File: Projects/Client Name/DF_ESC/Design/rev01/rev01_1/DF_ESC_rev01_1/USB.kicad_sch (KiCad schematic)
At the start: 9 parts, among them J8 USB_C_Receptacle_USB2.0, U10 PUSB3AB6Z

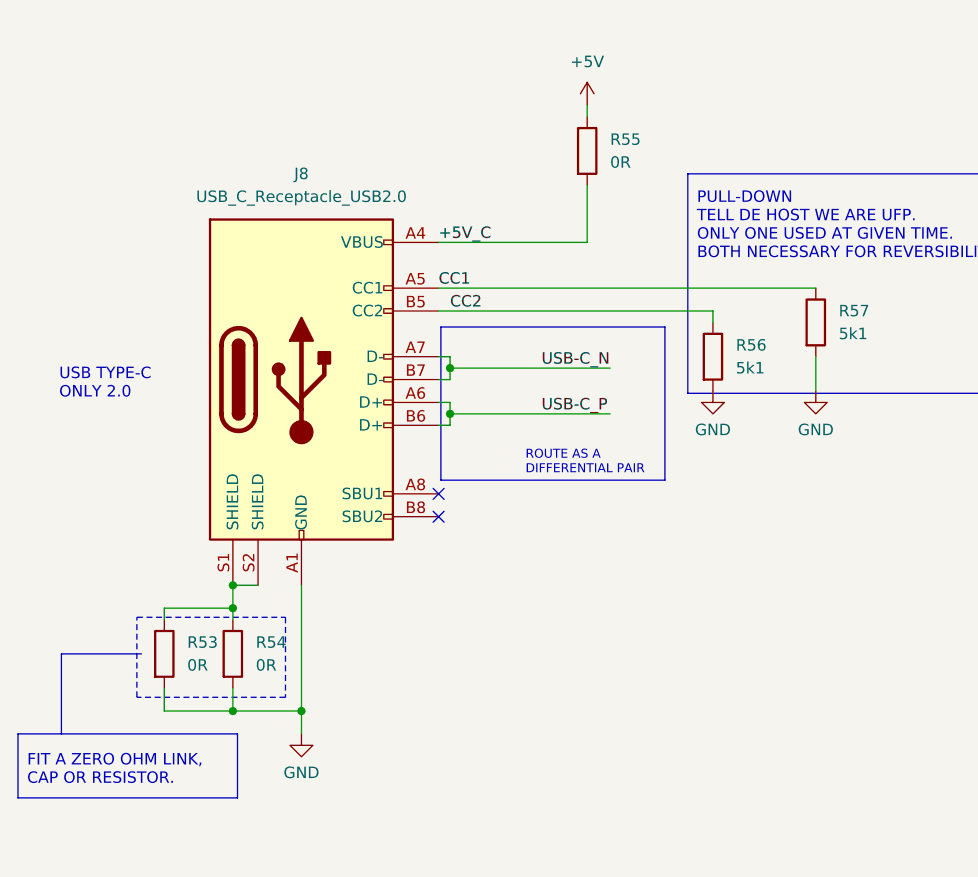
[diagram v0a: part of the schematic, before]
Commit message: update 20240427
Mejora de layout cero errores, solo falta añadir algunas reseñas en el silkscreen
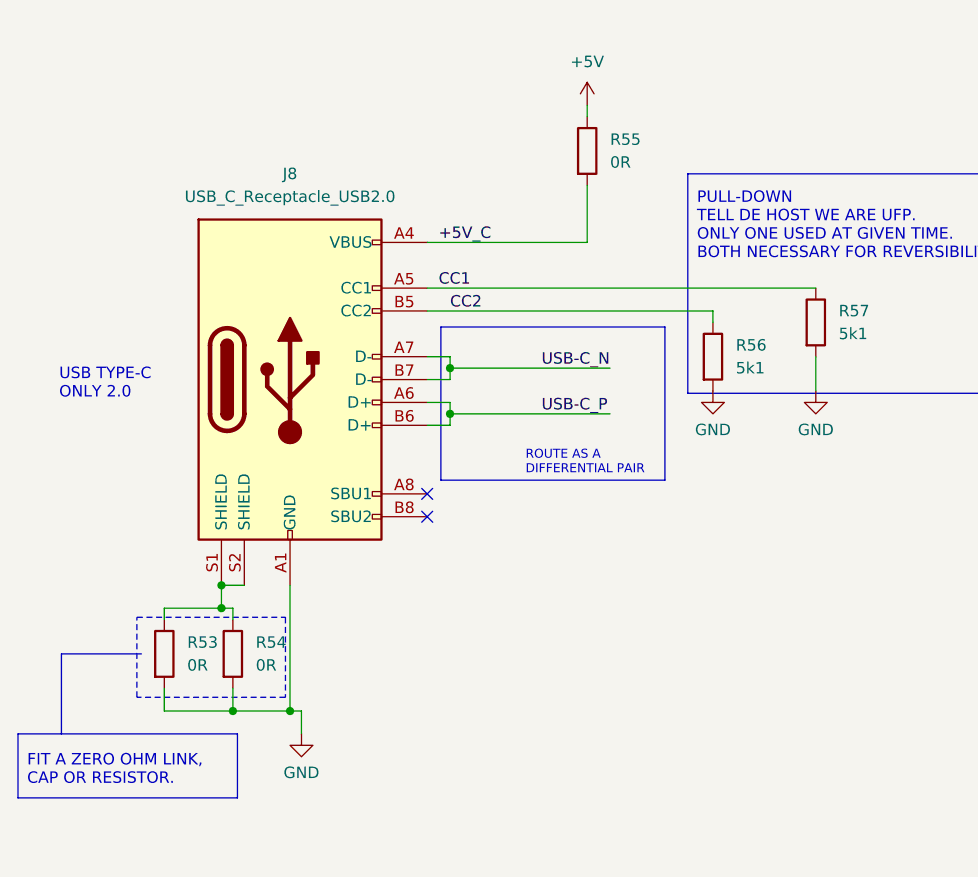
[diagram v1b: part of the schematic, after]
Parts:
- U10: footprint DF_ESC_Footprint_Library_Casa:XSON-7_L2.2-W1.2-P0.50-BL -> DF_ESC_Footprint_Library:XSON-7_L2.2-W1.2-P0.50-BL
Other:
- moved on the sheet: J8
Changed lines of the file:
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@@
-	)
-	(junction
-		(at 57.15 113.03)
-		(diameter 0)
-		(color 0 0 0 0)
-	)
-	(junction
-		(at 64.77 124.46)
-		(diameter 0)
-		(color 0 0 0 0)
 	)
 	(junction
@@
 	)
 	(junction
-		(at 57.15 110.49)
+		(at 55.88 113.03)
 		(diameter 0)
 		(color 0 0 0 0)
 	)
+	(junction
+		(at 63.5 124.46)
+		(diameter 0)
+		(color 0 0 0 0)
+	)
+	(junction
+		(at 55.88 110.49)
+		(diameter 0)
+		(color 0 0 0 0)
+	)
 	(no_connect
-		(at 80.01 100.33)
+		(at 78.74 100.33)
 	)
 	(no_connect
-		(at 80.01 102.87)
+		(at 78.74 102.87)
 	)
 	(wire
@@
 	(wire
 		(pts
-			(xy 81.28 87.63) (xy 80.01 87.63)
-		)
-		(stroke
-			(width 1)
-			(type default)
-			(color 194 0 0 1)
-		)
-	)
-	(wire
-		(pts
-			(xy 80.01 85.09) (xy 81.28 85.09)
+			(xy 55.88 113.03) (xy 57.15 113.03)
+		)
+		(stroke
+			(width 0)
+			(type default)
+		)
+	)
+	(wire
+		(pts
+			(xy 81.28 87.63) (xy 78.74 87.63)
+		)
+		(stroke
+			(width 1)
+			(type default)
+			(color 194 0 0 1)
+		)
+	)
+	(wire
+		(pts
+			(xy 55.88 110.49) (xy 58.42 110.49)
+		)
+		(stroke
+			(width 0)
+			(type default)
+		)
+	)
+	(wire
+		(pts
+			(xy 78.74 85.09) (xy 81.28 85.09)
 		)
 		(stroke
@@
 	(wire
 		(pts
-			(xy 80.01 72.39) (xy 96.52 72.39)
-		)
-		(stroke
-			(width 0)
-			(type default)
-		)
-	)
-	(wire
-		(pts
 			(xy 57.15 114.3) (xy 57.15 113.03)
 		)
@@
 	(wire
 		(pts
-			(xy 81.28 92.71) (xy 80.01 92.71)
+			(xy 78.74 72.39) (xy 96.52 72.39)
+		)
+		(stroke
+			(width 0)
+			(type default)
+		)
+	)
+	(wire
+		(pts
+			(xy 63.5 124.46) (xy 57.15 124.46)
+		)
+		(stroke
+			(width 0)
+			(type default)
+		)
+	)
+	(wire
+		(pts
+			(xy 81.28 92.71) (xy 78.74 92.71)
 		)
 		(stroke
@@
 	(wire
 		(pts
+			(xy 55.88 110.49) (xy 55.88 113.03)
+		)
+		(stroke
+			(width 0)
+			(type default)
+		)
+	)
+	(wire
+		(pts
 			(xy 81.28 91.44) (xy 81.28 92.71)
 		)
@@
 	(wire
 		(pts
-			(xy 64.77 110.49) (xy 64.77 124.46)
+			(xy 63.5 110.49) (xy 63.5 124.46)
 		)
 		(stroke
@@
 	(wire
 		(pts
-			(xy 49.53 113.03) (xy 57.15 113.03)
-		)
-		(stroke
-			(width 0)
-			(type default)
-		)
-	)
-	(wire
-		(pts
-			(xy 80.01 90.17) (xy 81.28 90.17)
+			(xy 49.53 113.03) (xy 55.88 113.03)
+		)
+		(stroke
+			(width 0)
+			(type default)
+		)
+	)
+	(wire
+		(pts
+			(xy 78.74 90.17) (xy 81.28 90.17)
 		)
 		(stroke
@@
 	(wire
 		(pts
-			(xy 57.15 110.49) (xy 57.15 113.03)
-		)
-		(stroke
-			(width 0)
-			(type default)
-		)
-	)
-	(wire
-		(pts
 			(xy 81.28 86.36) (xy 99.06 86.36)
 		)
@@
 	(wire
 		(pts
-			(xy 80.01 80.01) (xy 110.49 80.01)
+			(xy 78.74 80.01) (xy 110.49 80.01)
 		)
 		(stroke
@@
 	(wire
 		(pts
-			(xy 57.15 110.49) (xy 59.944 110.49)
-		)
-		(stroke
-			(width 0)
-			(type default)
-		)
-	)
-	(wire
-		(pts
-			(xy 64.77 124.46) (xy 57.15 124.46)
+			(xy 64.77 124.46) (xy 63.5 124.46)
 		)
 		(stroke
@@
 	(wire
 		(pts
-			(xy 80.01 77.47) (xy 121.92 77.47)
+			(xy 78.74 77.47) (xy 121.92 77.47)
 		)
 		(stroke
@@
 	(symbol
 		(lib_id "DF_ESC_Symbol_Library_Casa:USB_C_Receptacle_USB2.0")
-		(at 64.77 87.63 0)
+		(at 63.5 87.63 0)
 		(unit 1)
 		(exclude_from_sim no)
@@
 		(fields_autoplaced yes)
 		(property "Reference" "J8"
-			(at 64.77 64.77 0)
+			(at 63.5 64.77 0)
 			(effects
 				(font
@@
 		)
 		(property "Value" "USB_C_Receptacle_USB2.0"
-			(at 64.77 67.31 0)
+			(at 63.5 67.31 0)
 			(effects
 				(font
@@
 		)
 		(property "Footprint" "DF_ESC_Footprint_Library_Casa:USB-C_SMD-TYPE-C-31-M-12"
-			(at 83.82 61.976 0)
+			(at 82.55 61.976 0)
 			(effects
 				(font
@@
 		)
 		(property "Datasheet" "https://www.usb.org/sites/default/files/documents/usb_type-c.zip"
-			(at 87.884 64.516 0)
+			(at 86.614 64.516 0)
 			(effects
 				(font
@@
 		)
 		(property "Description" ""
-			(at 64.77 87.63 0)
+			(at 63.5 87.63 0)
 			(effects
 				(font
@@
 			)
 		)
-		(property "Footprint" "DF_ESC_Footprint_Library_Casa:XSON-7_L2.2-W1.2-P0.50-BL"
+		(property "Footprint" "DF_ESC_Footprint_Library:XSON-7_L2.2-W1.2-P0.50-BL"
 			(at 186.69 109.22 0)
 			(effects
